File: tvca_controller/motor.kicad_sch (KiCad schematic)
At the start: 8 parts, among them J3 4DB-P108-02, J4 PT 1,5/ 4-5,0-H, J5 4DB-P108-02

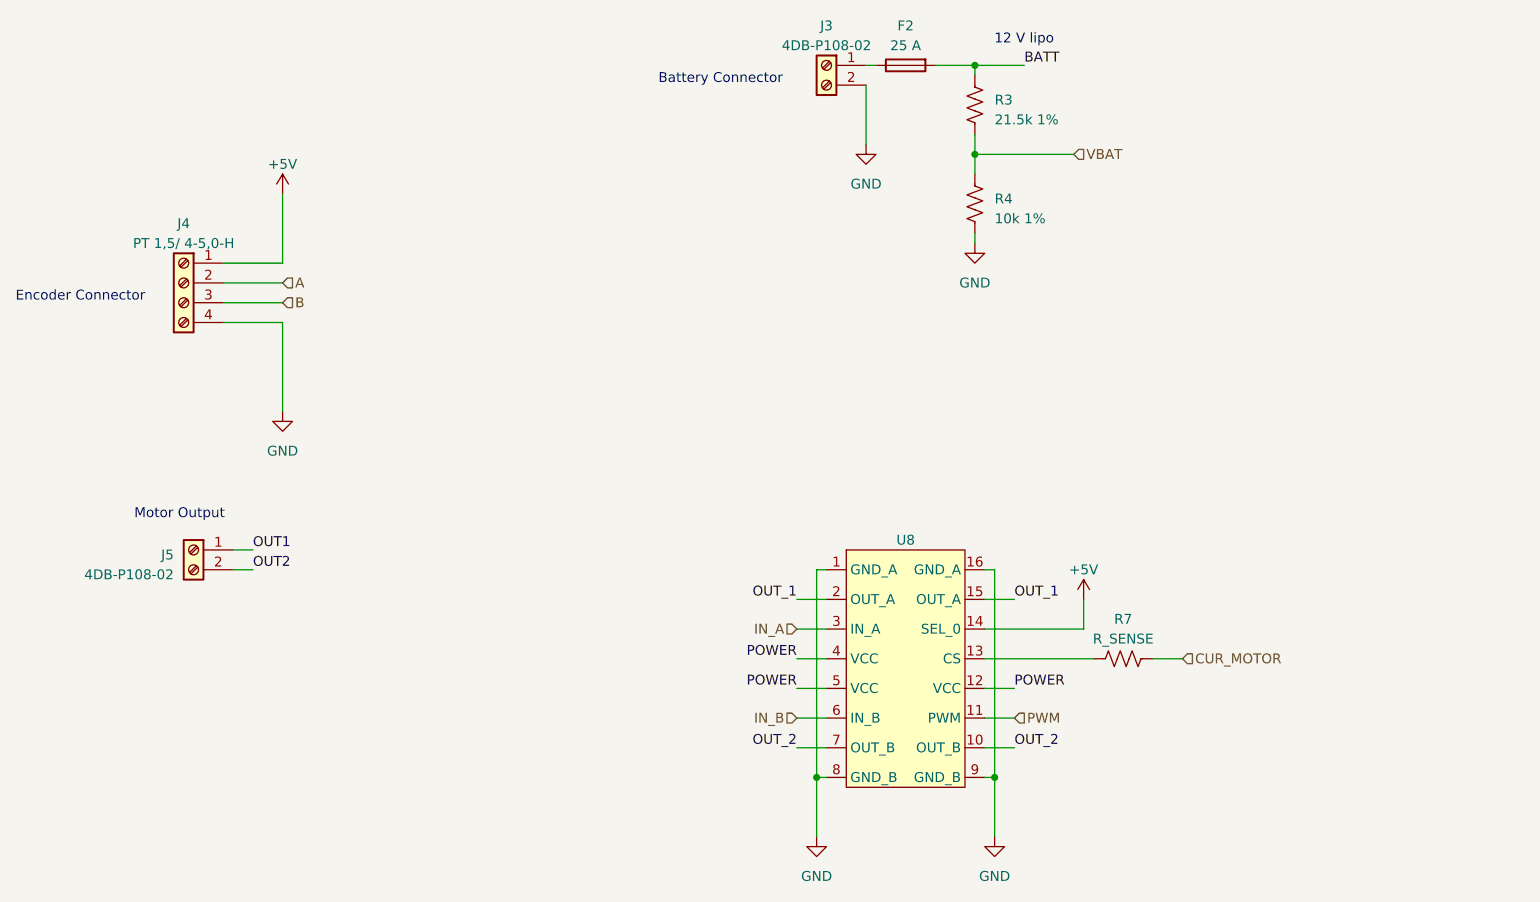
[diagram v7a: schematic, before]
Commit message: Update motor controller IC and fuse holders
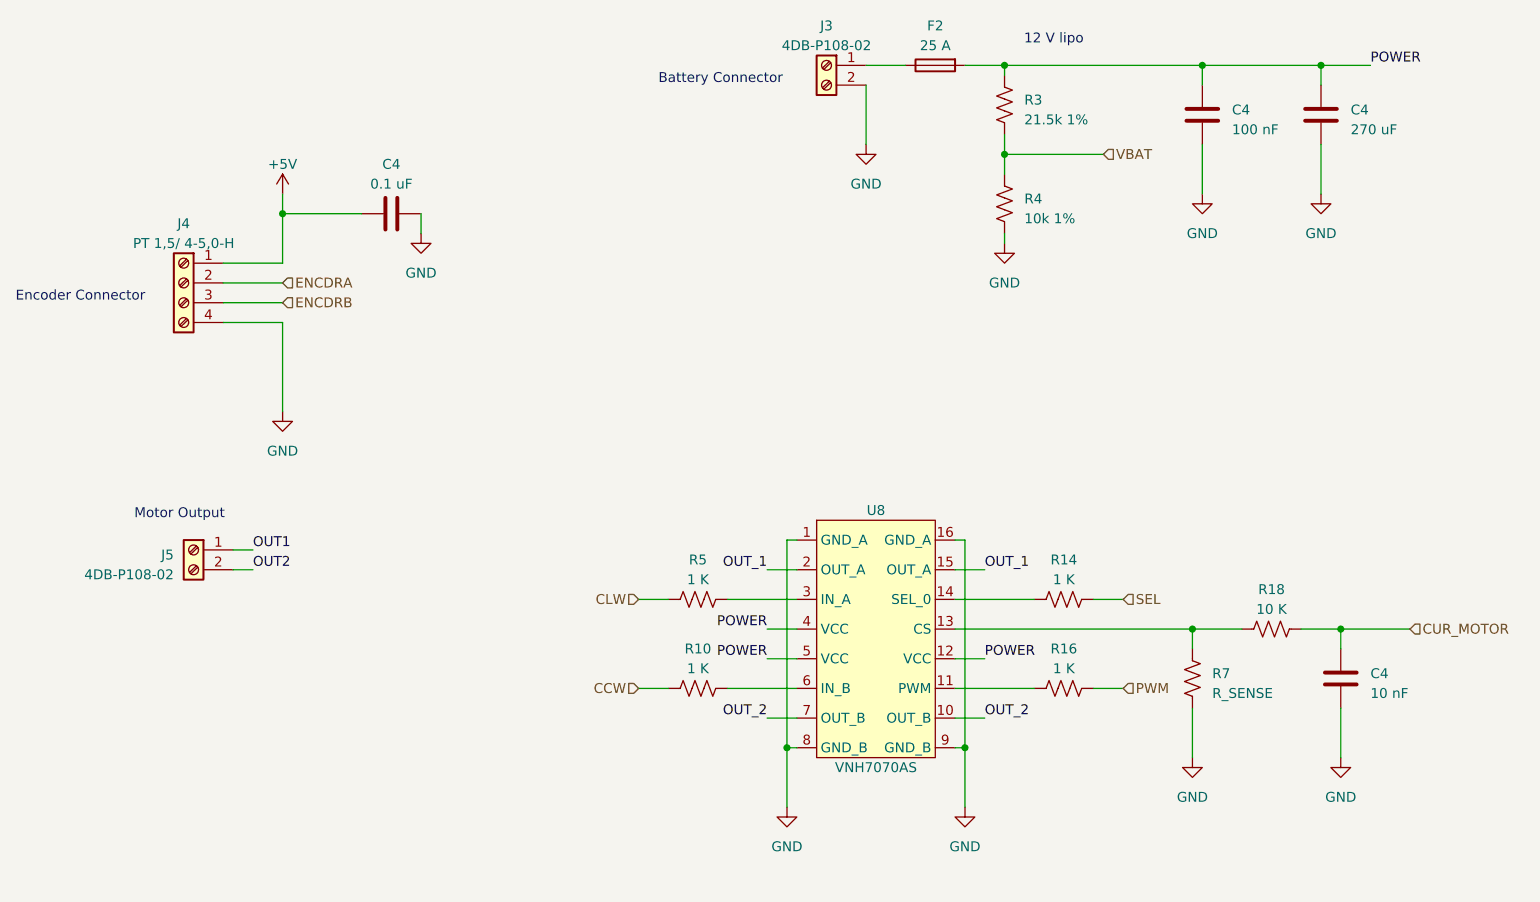
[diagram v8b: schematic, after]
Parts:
- added C4: 100 nF, Capacitor_SMD:C_0805_2012Metric_Pad1.18x1.45mm_HandSolder, symbol Device:C
- added C4: 10 nF, Capacitor_SMD:C_0805_2012Metric_Pad1.18x1.45mm_HandSolder, symbol Device:C
- added C4: 270 uF, Capacitor_SMD:C_0805_2012Metric_Pad1.18x1.45mm_HandSolder, symbol Device:C
- added C4: 0.1 uF, Capacitor_SMD:C_0805_2012Metric_Pad1.18x1.45mm_HandSolder, symbol Device:C
- added R10, R14, R16, R5: 1 K, Resistor_SMD:R_0805_2012Metric_Pad1.20x1.40mm_HandSolder, symbol Device:R_US
- added R18: 10 K, Resistor_SMD:R_0805_2012Metric_Pad1.20x1.40mm_HandSolder, symbol Device:R_US
- F2: footprint Fuse:Fuseholder_Cylinder-6.3x32mm_Schurter_0031-8002_Horizontal_Open -> Fuse:Fuseholder_Keystone_3555-2
- U8: value ~ -> VNH7070AS
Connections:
- net BATT is gone; now on net POWER: F2.2, R3.1
- net +5V: now also C4.1; no longer U8.14 (SEL_0)
- net CUR_MOTOR: now also C4.1, R18.1; no longer R7.1
- net GND: now also R7.2, C4.2, C4.2, C4.2, C4.2
- net POWER: now also C4.1, C4.1
- net PWM: now also R16.1; no longer U8.11 (PWM)
- net at U8.13 (CS): now also R7.1, R18.2; no longer R7.2
- net A renamed ENCDRA
- net B renamed ENCDRB
- net IN_A: no longer names the net of U8.3 (IN_A)
- net IN_A: now also R5.1
- net IN_B: no longer names the net of U8.6 (IN_B)
- net IN_B: now also R10.1
- new net: R16.2, U8.11 (PWM)
- new net: R14.2, U8.14 (SEL_0)
- new net CCW: R10.2
- new net CLW: R5.2
- new net SEL: R14.1
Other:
- moved on the sheet: F2, R3, R4, R7, U8
